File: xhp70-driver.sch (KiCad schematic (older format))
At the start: 27 parts, among them J1 LEMO2, J2 AVR-ISP-6, Q1 Q_NMOS_GDS, U1 AL8871Q, U2 ATtiny85-20SU, U3 L7805

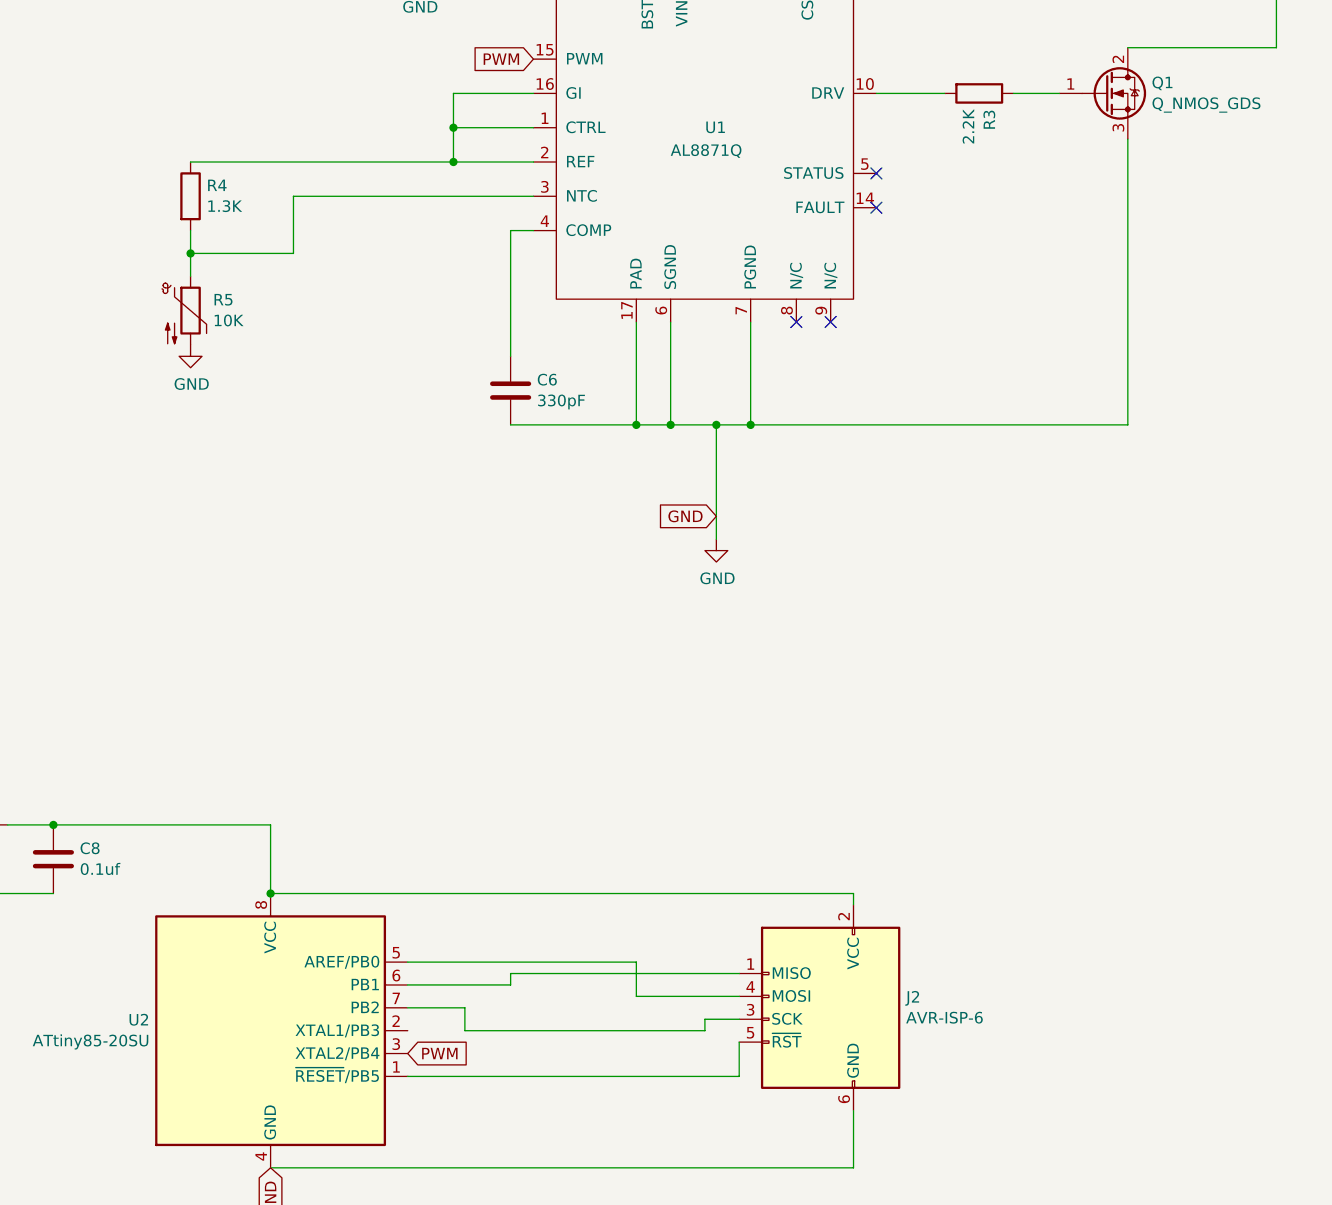
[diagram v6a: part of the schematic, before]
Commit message: Rev 2a - route NTC Thermistor to Attiny to control output
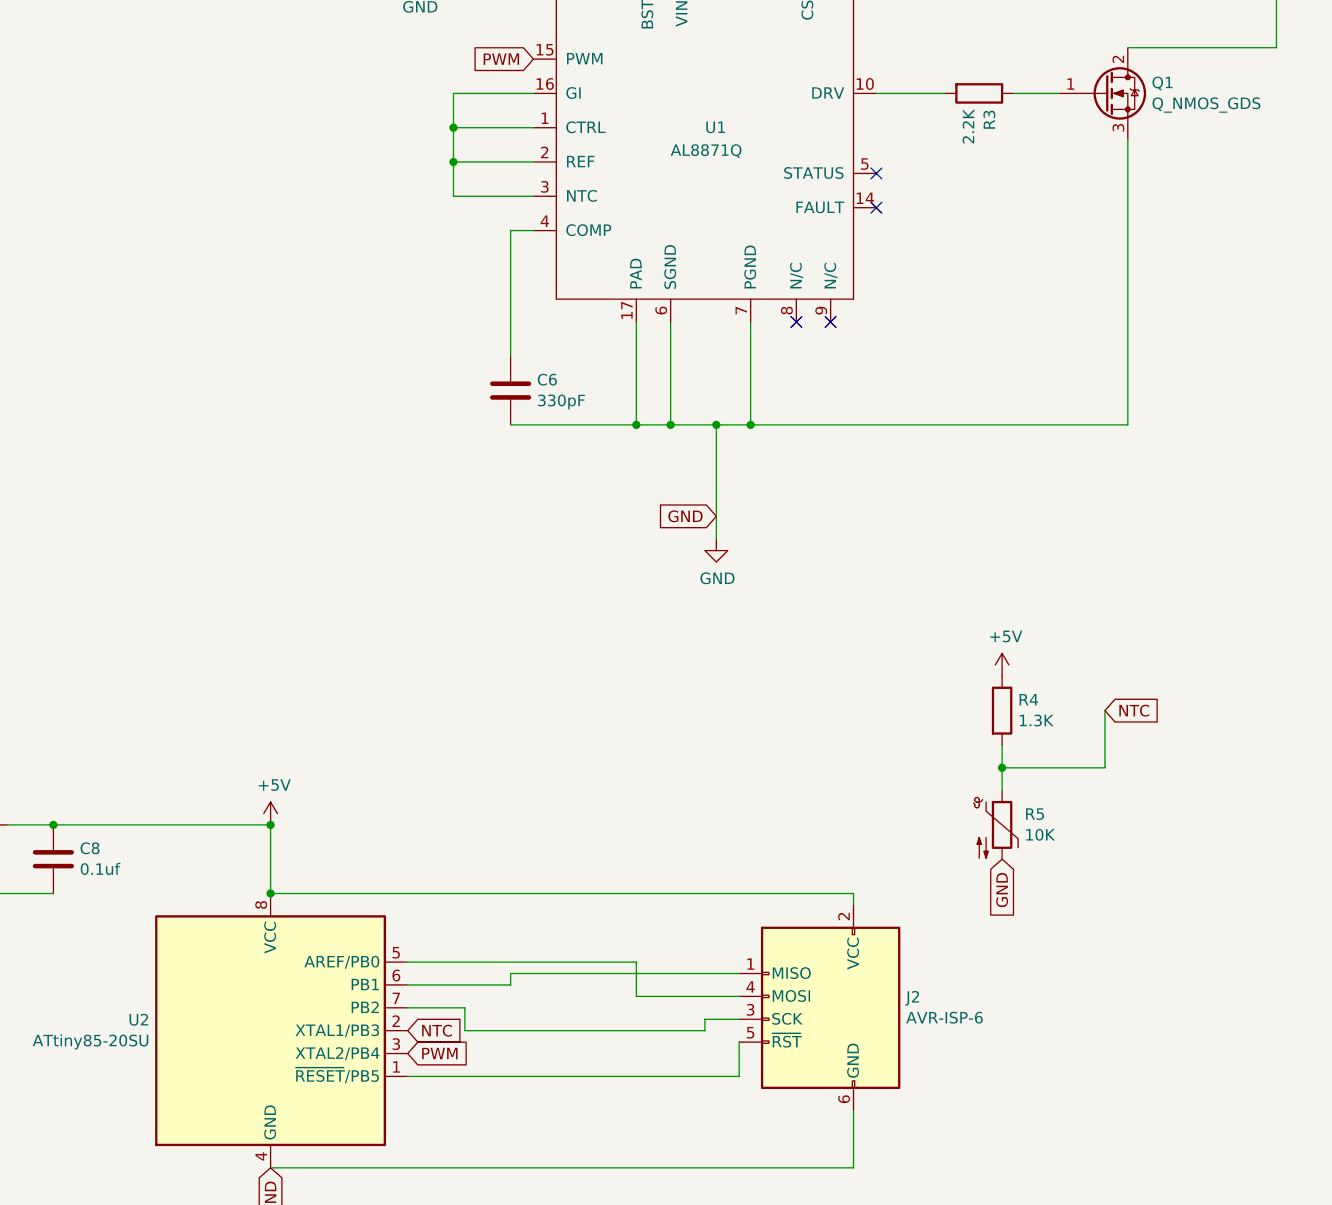
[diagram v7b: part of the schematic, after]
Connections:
- net NTC: now reaches R4.2, R5.1
- net NTC: now also U2.2 (XTAL1/PB3); no longer U1.3 (NTC)
- net at U1.1 (CTRL), U1.16 (GI), U1.2 (REF): now also U1.3 (NTC); no longer R4.1
- net +5V: now reaches C8.1, J2.2 (VCC), U2.8 (VCC), U3.3 (OUT)
- net +5V: now also R4.1
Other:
- moved on the sheet: R4, R5
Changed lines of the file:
@@
 L Device:Thermistor_NTC R5
 U 1 1 6030A23F
-P 2900 3400
-F 0 "R5" H 2998 3446 50  0000 L CNN
-F 1 "10K" H 2998 3355 50  0000 L CNN
-F 2 "Connector_JST:JST_SH_BM02B-SRSS-TB_1x02-1MP_P1.00mm_Vertical" H 2900 3450 50  0001 C CNN
-F 3 "~" H 2900 3450 50  0001 C CNN
-	1    2900 3400
+P 6450 5650
+F 0 "R5" H 6548 5696 50  0000 L CNN
+F 1 "10K" H 6548 5605 50  0000 L CNN
+F 2 "Connector_JST:JST_SH_BM02B-SRSS-TB_1x02-1MP_P1.00mm_Vertical" H 6450 5700 50  0001 C CNN
+F 3 "~" H 6450 5700 50  0001 C CNN
+	1    6450 5650
 	1    0    0    -1
 $EndComp
@@
 L Device:R R4
 U 1 1 6031B105
-P 2900 2900
-F 0 "R4" H 2970 2946 50  0000 L CNN
-F 1 "1.3K" H 2970 2855 50  0000 L CNN
-F 2 "Resistor_SMD:R_0805_2012Metric" V 2830 2900 50  0001 C CNN
-F 3 "~" H 2900 2900 50  0001 C CNN
-	1    2900 2900
+P 6450 5150
+F 0 "R4" H 6520 5196 50  0000 L CNN
+F 1 "1.3K" H 6520 5105 50  0000 L CNN
+F 2 "Resistor_SMD:R_0805_2012Metric" V 6380 5150 50  0001 C CNN
+F 3 "~" H 6450 5150 50  0001 C CNN
+	1    6450 5150
 	1    0    0    -1
 $EndComp
@@
 Connection ~ 4250 1850
 Wire Wire Line
-	2900 2750 4050 2750
-Wire Wire Line
-	2900 3050 2900 3150
-$Comp
-L power:GND #PWR0104
-U 1 1 6041CD87
-P 2900 3550
-F 0 "#PWR0104" H 2900 3300 50  0001 C CNN
-F 1 "GND" H 2905 3377 50  0000 C CNN
-F 2 "" H 2900 3550 50  0001 C CNN
-F 3 "" H 2900 3550 50  0001 C CNN
-	1    2900 3550
-	1    0    0    -1
-$EndComp
-Wire Wire Line
-	2900 3150 3350 3150
-Wire Wire Line
-	3350 3150 3350 2900
-Wire Wire Line
-	3350 2900 4400 2900
-Connection ~ 2900 3150
-Wire Wire Line
-	2900 3150 2900 3250
+	6450 5300 6450 5400
+Wire Wire Line
+	6450 5400 6900 5400
+Wire Wire Line
+	6900 5400 6900 5150
+Connection ~ 6450 5400
+Wire Wire Line
+	6450 5400 6450 5500
 Wire Wire Line
 	4400 2450 4050 2450
 Wire Wire Line
 	4050 2450 4050 2600
-Connection ~ 4050 2750
 Wire Wire Line
 	4050 2750 4400 2750
@@
 Wire Wire Line
 	1200 5950 1800 5950
+Wire Wire Line
+	4050 2750 4050 2900
+Wire Wire Line
+	4050 2900 4400 2900
+Connection ~ 4050 2750
+$Comp
+L power:+5V #PWR?
+U 1 1 6047367D
+P 3250 5650
+F 0 "#PWR?" H 3250 5500 50  0001 C CNN
+F 1 "+5V" H 3265 5823 50  0000 C CNN
+F 2 "" H 3250 5650 50  0001 C CNN
+F 3 "" H 3250 5650 50  0001 C CNN
+	1    3250 5650
+	1    0    0    -1
+$EndComp
+Connection ~ 3250 5650
+$Comp
+L power:+5V #PWR?
+U 1 1 60473F1D
+P 6450 5000
+F 0 "#PWR?" H 6450 4850 50  0001 C CNN
+F 1 "+5V" H 6465 5173 50  0000 C CNN
+F 2 "" H 6450 5000 50  0001 C CNN
+F 3 "" H 6450 5000 50  0001 C CNN
+	1    6450 5000
+	1    0    0    -1
+$EndComp
+Text GLabel 6450 5800 3    50   Input ~ 0
+GND
+Text GLabel 6900 5150 2    50   Input ~ 0
+NTC
+Text GLabel 3850 6550 2    50   Input ~ 0
+NTC
 $EndSCHEMATC

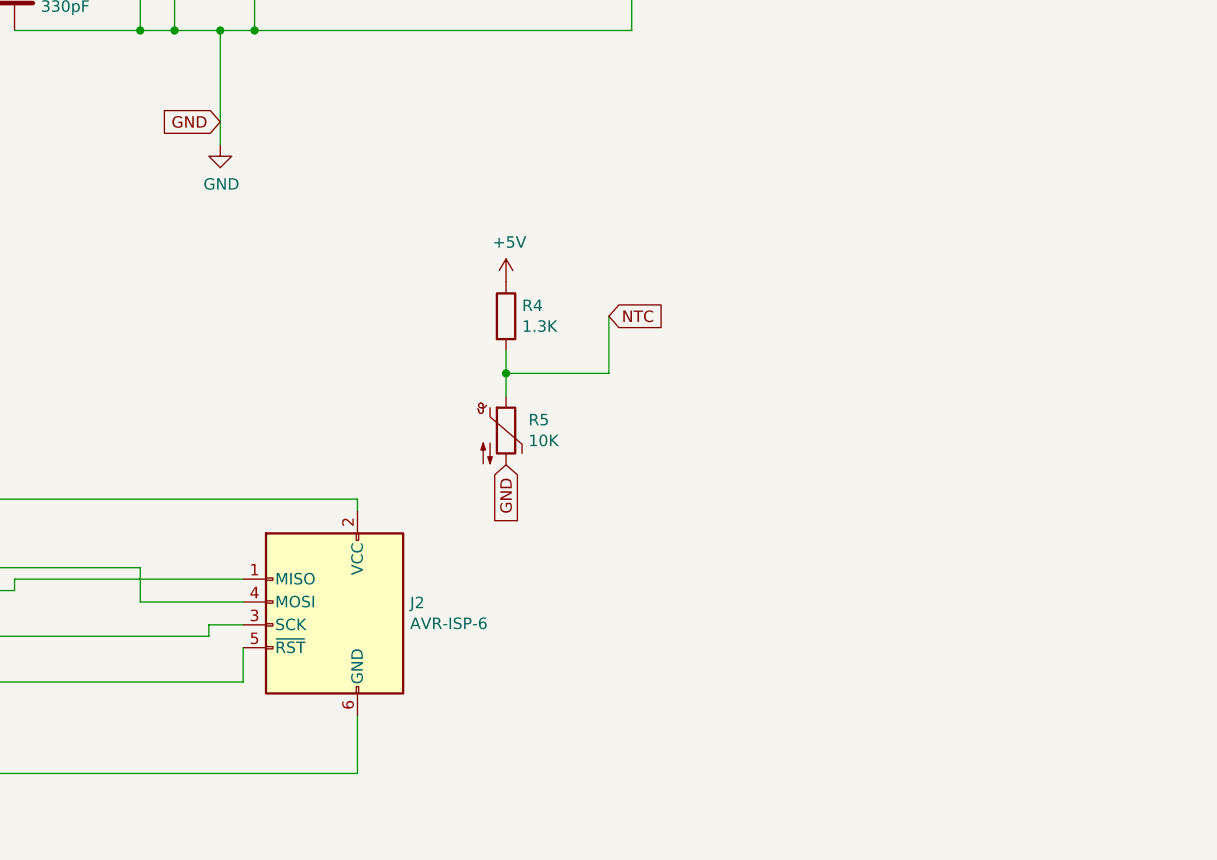
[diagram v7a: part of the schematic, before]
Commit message: L7805 schematic pinout is wrong. Needs reroute. `
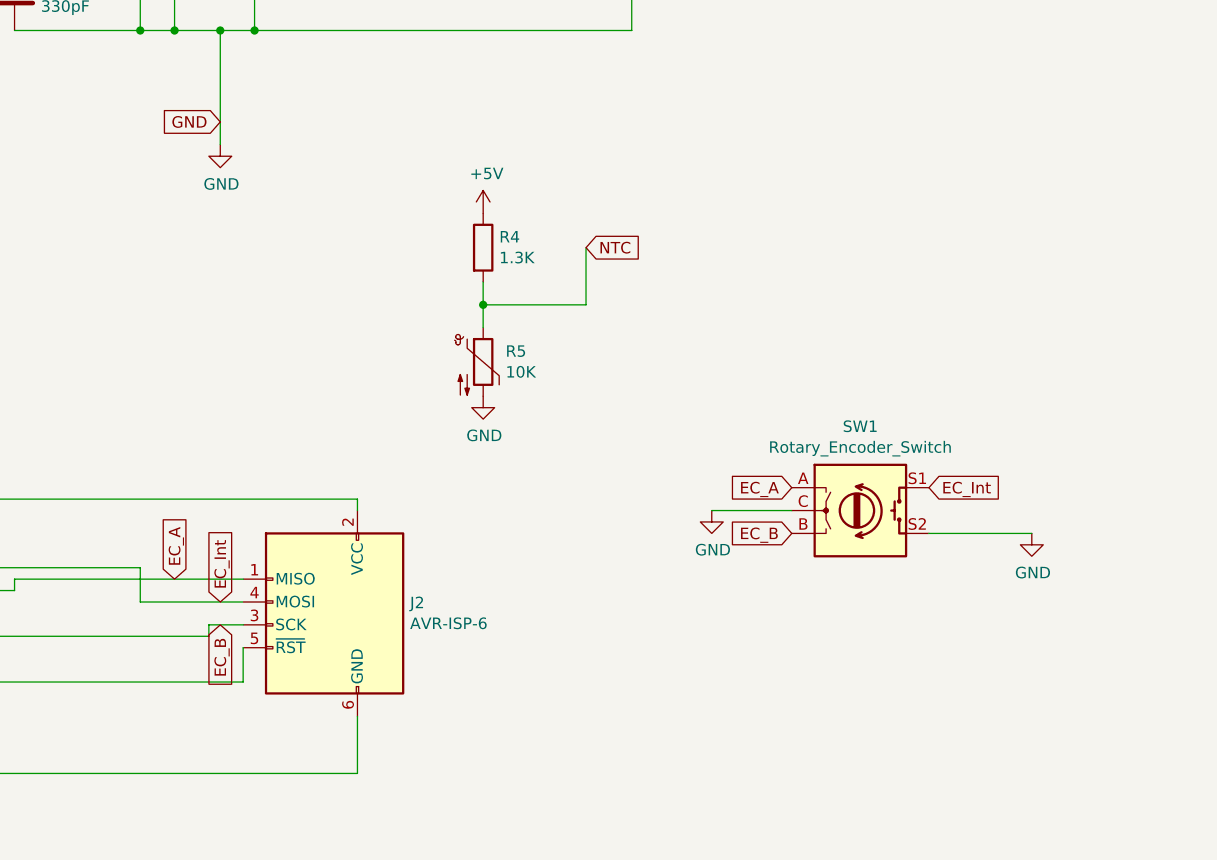
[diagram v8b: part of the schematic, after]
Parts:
- added SW1: Rotary_Encoder_Switch, symbol Device:Rotary_Encoder_Switch
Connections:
- net GND: now also SW1.C, SW1.S2
- net EC_Int: now reaches J2.4 (MOSI), U2.5 (AREF/PB0)
- net EC_Int: now also SW1.S1
- net EC_A: now reaches J2.1 (MISO), U2.6 (PB1)
- net EC_A: now also SW1.A
- net EC_B: now reaches J2.3 (SCK), U2.7 (PB2)
- net EC_B: now also SW1.B
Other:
- moved on the sheet: R4, R5
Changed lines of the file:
@@
 L Device:Thermistor_NTC R5
 U 1 1 6030A23F
-P 6450 5650
-F 0 "R5" H 6548 5696 50  0000 L CNN
-F 1 "10K" H 6548 5605 50  0000 L CNN
-F 2 "Connector_JST:JST_SH_BM02B-SRSS-TB_1x02-1MP_P1.00mm_Vertical" H 6450 5700 50  0001 C CNN
-F 3 "~" H 6450 5700 50  0001 C CNN
-	1    6450 5650
+P 6350 5350
+F 0 "R5" H 6448 5396 50  0000 L CNN
+F 1 "10K" H 6448 5305 50  0000 L CNN
+F 2 "Connector_JST:JST_SH_BM02B-SRSS-TB_1x02-1MP_P1.00mm_Vertical" H 6350 5400 50  0001 C CNN
+F 3 "~" H 6350 5400 50  0001 C CNN
+	1    6350 5350
 	1    0    0    -1
 $EndComp
@@
 L Device:R R4
 U 1 1 6031B105
-P 6450 5150
-F 0 "R4" H 6520 5196 50  0000 L CNN
-F 1 "1.3K" H 6520 5105 50  0000 L CNN
-F 2 "Resistor_SMD:R_0805_2012Metric" V 6380 5150 50  0001 C CNN
-F 3 "~" H 6450 5150 50  0001 C CNN
-	1    6450 5150
+P 6350 4850
+F 0 "R4" H 6420 4896 50  0000 L CNN
+F 1 "1.3K" H 6420 4805 50  0000 L CNN
+F 2 "Resistor_SMD:R_0805_2012Metric" V 6280 4850 50  0001 C CNN
+F 3 "~" H 6350 4850 50  0001 C CNN
+	1    6350 4850
 	1    0    0    -1
 $EndComp
@@
 Connection ~ 4250 1850
 Wire Wire Line
-	6450 5300 6450 5400
-Wire Wire Line
-	6450 5400 6900 5400
-Wire Wire Line
-	6900 5400 6900 5150
-Connection ~ 6450 5400
-Wire Wire Line
-	6450 5400 6450 5500
+	6350 5000 6350 5100
+Wire Wire Line
+	6350 5100 6800 5100
+Wire Wire Line
+	6800 5100 6800 4850
+Connection ~ 6350 5100
+Wire Wire Line
+	6350 5100 6350 5200
 Wire Wire Line
 	4400 2450 4050 2450
@@
 Connection ~ 4050 2750
 $Comp
-L power:+5V #PWR?
+L power:+5V #PWR0104
 U 1 1 6047367D
 P 3250 5650
-F 0 "#PWR?" H 3250 5500 50  0001 C CNN
+F 0 "#PWR0104" H 3250 5500 50  0001 C CNN
 F 1 "+5V" H 3265 5823 50  0000 C CNN
 F 2 "" H 3250 5650 50  0001 C CNN
@@
 Connection ~ 3250 5650
 $Comp
-L power:+5V #PWR?
+L power:+5V #PWR0105
 U 1 1 60473F1D
-P 6450 5000
-F 0 "#PWR?" H 6450 4850 50  0001 C CNN
-F 1 "+5V" H 6465 5173 50  0000 C CNN
-F 2 "" H 6450 5000 50  0001 C CNN
-F 3 "" H 6450 5000 50  0001 C CNN
-	1    6450 5000
-	1    0    0    -1
-$EndComp
-Text GLabel 6450 5800 3    50   Input ~ 0
-GND
-Text GLabel 6900 5150 2    50   Input ~ 0
+P 6350 4700
+F 0 "#PWR0105" H 6350 4550 50  0001 C CNN
+F 1 "+5V" H 6365 4873 50  0000 C CNN
+F 2 "" H 6350 4700 50  0001 C CNN
+F 3 "" H 6350 4700 50  0001 C CNN
+	1    6350 4700
+	1    0    0    -1
+$EndComp
+Text GLabel 6800 4850 2    50   Input ~ 0
 NTC
 Text GLabel 3850 6550 2    50   Input ~ 0
 NTC
+$Comp
+L Device:Rotary_Encoder_Switch SW1
+U 1 1 604AD982
+P 8000 6000
+F 0 "SW1" H 8000 6367 50  0000 C CNN
+F 1 "Rotary_Encoder_Switch" H 8000 6276 50  0000 C CNN
+F 2 "" H 7850 6160 50  0001 C CNN
+F 3 "~" H 8000 6260 50  0001 C CNN
+	1    8000 6000
+	1    0    0    -1
+$EndComp
+Text GLabel 8300 5900 2    50   Input ~ 0
+EC_Int
+Wire Wire Line
+	8300 6100 8750 6100
+Text GLabel 5200 6400 1    50   Input ~ 0
+EC_Int
+Text GLabel 7700 5900 0    50   Input ~ 0
+EC_A
+Wire Wire Line
+	7350 6000 7700 6000
+Text GLabel 7700 6100 0    50   Input ~ 0
+EC_B
+Text GLabel 5000 6300 1    50   Input ~ 0
+EC_A
+Text GLabel 5200 6500 3    50   Input ~ 0
+EC_B
+$Comp
+L power:GND #PWR?
+U 1 1 604E195D
+P 6350 5500
+F 0 "#PWR?" H 6350 5250 50  0001 C CNN
+F 1 "GND" H 6355 5327 50  0000 C CNN
+F 2 "" H 6350 5500 50  0001 C CNN
+F 3 "" H 6350 5500 50  0001 C CNN
+	1    6350 5500
+	1    0    0    -1
+$EndComp
+$Comp
+L power:GND #PWR?
+U 1 1 604F3390
+P 7350 6000
+F 0 "#PWR?" H 7350 5750 50  0001 C CNN
+F 1 "GND" H 7355 5827 50  0000 C CNN
+F 2 "" H 7350 6000 50  0001 C CNN
+F 3 "" H 7350 6000 50  0001 C CNN
+	1    7350 6000
+	1    0    0    -1
+$EndComp
+$Comp
+L power:GND #PWR?
+U 1 1 604F37B3
+P 8750 6100
+F 0 "#PWR?" H 8750 5850 50  0001 C CNN
+F 1 "GND" H 8755 5927 50  0000 C CNN
+F 2 "" H 8750 6100 50  0001 C CNN
+F 3 "" H 8750 6100 50  0001 C CNN
+	1    8750 6100
+	1    0    0    -1
+$EndComp
 $EndSCHEMATC
